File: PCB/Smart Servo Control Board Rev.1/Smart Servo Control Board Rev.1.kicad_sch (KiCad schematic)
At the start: 39 parts

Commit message: salvataggio layout board
tornare a questo salvataggio per riprovare.
piani potenza interni e piani segnali esterni, da scambiare ?
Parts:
- removed J? (x2): CTRL, symbol Connector:Conn_01x04_Female
- removed J?: PRGR, symbol Connector:Conn_01x04_Female
- added J1: PRGR, Connector_PinSocket_2.54mm:PinSocket_1x04_P2.54mm_Vertical, symbol Connector:Conn_01x04_Female
- added J2, J3: CTRL, Connector_PinSocket_2.54mm:PinSocket_1x04_P2.54mm_Vertical, symbol Connector:Conn_01x04_Female
- C1, C10, C11, C12, C14, C2, C3, C4, C5, C6, C7, C8, C9: renamed from C?; footprint Capacitor_SMD:C_0603_1608Metric -> Capacitor_SMD:C_0603_1608Metric_Pad1.08x0.95mm_HandSolder
- C13: renamed from C?; footprint (none) -> Capacitor_SMD:C_0603_1608Metric_Pad1.08x0.95mm_HandSolder
- J4, J5: renamed from J?; footprint (none) -> Connector_PinSocket_2.54mm:PinSocket_1x01_P2.54mm_Vertical
- R1, R2, R3, R5, R6, R7, R8, R9: renamed from R?; footprint (none) -> Resistor_SMD:R_0603_1608Metric_Pad0.98x0.95mm_HandSolder
- R4: renamed from R?; footprint (none) -> Resistor_SMD:R_1206_3216Metric_Pad1.30x1.75mm_HandSolder
- U5, U6, U7: renamed from U?; footprint (none) -> Package_SO:SOIC-8_3.9x4.9mm_P1.27mm
- gave numbers to parts that had none: 6
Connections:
- net +3V3: now also C11.2, C12.2, U4.2 (A0); no longer C11.1, C12.1, U4.1 (A1)
- net +5V: now also J1.4 (Pin_4), J2.4 (Pin_4), J3.4 (Pin_4)
- net A: now also U2.29 (PA8)
- net B: now also U2.31 (PA10)
- net GNDD: now also C11.1, C12.1, U4.1 (A1), J1.1 (Pin_1), J2.1 (Pin_1), J3.1 (Pin_1); no longer C11.2, C12.2, U4.2 (A0)
- net SCL1: now also U2.42 (PB6)
- net SCL2: now also U2.21 (PB10), J2.3 (Pin_3), J3.3 (Pin_3)
- net SDA1: now also U2.43 (PB7)
- net SDA2: now also U2.22 (PB11), J2.2 (Pin_2), J3.2 (Pin_2)
- net SWDCLK: now also J1.2 (Pin_2)
- net SWDIO: now also J1.3 (Pin_3)
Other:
- moved on the sheet: C11, C12

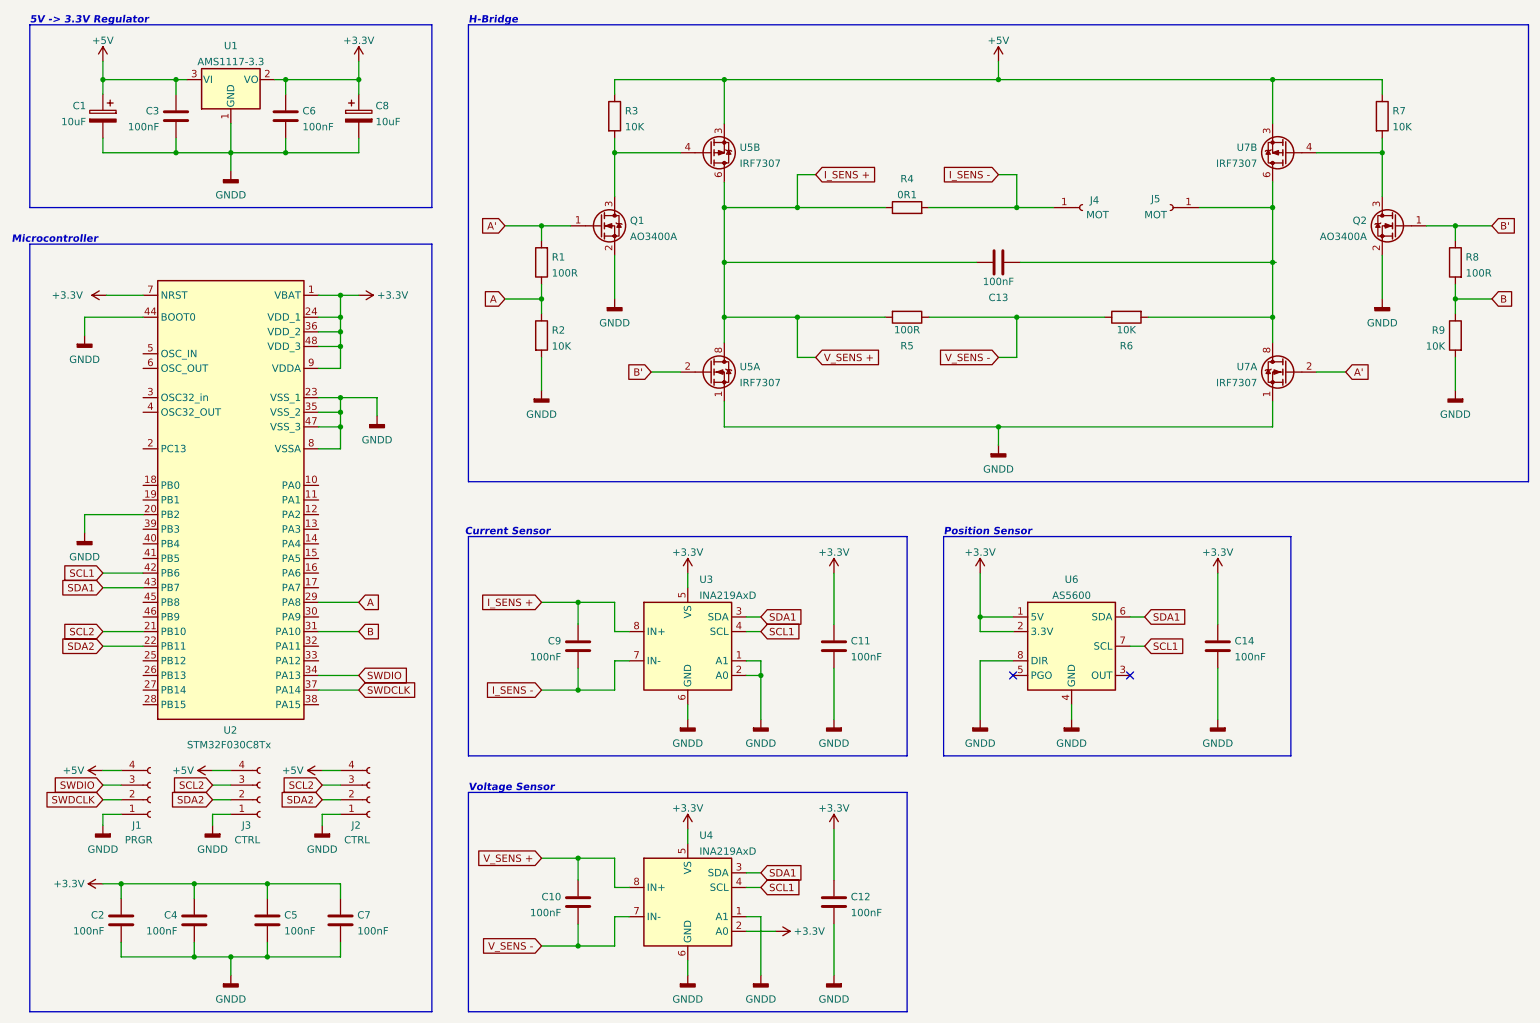
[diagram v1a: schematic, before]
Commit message: Prima versione definitiva PCB
tracciate le piste nel modo migliore possibile per ora, resta da sistemare il silkscreen.
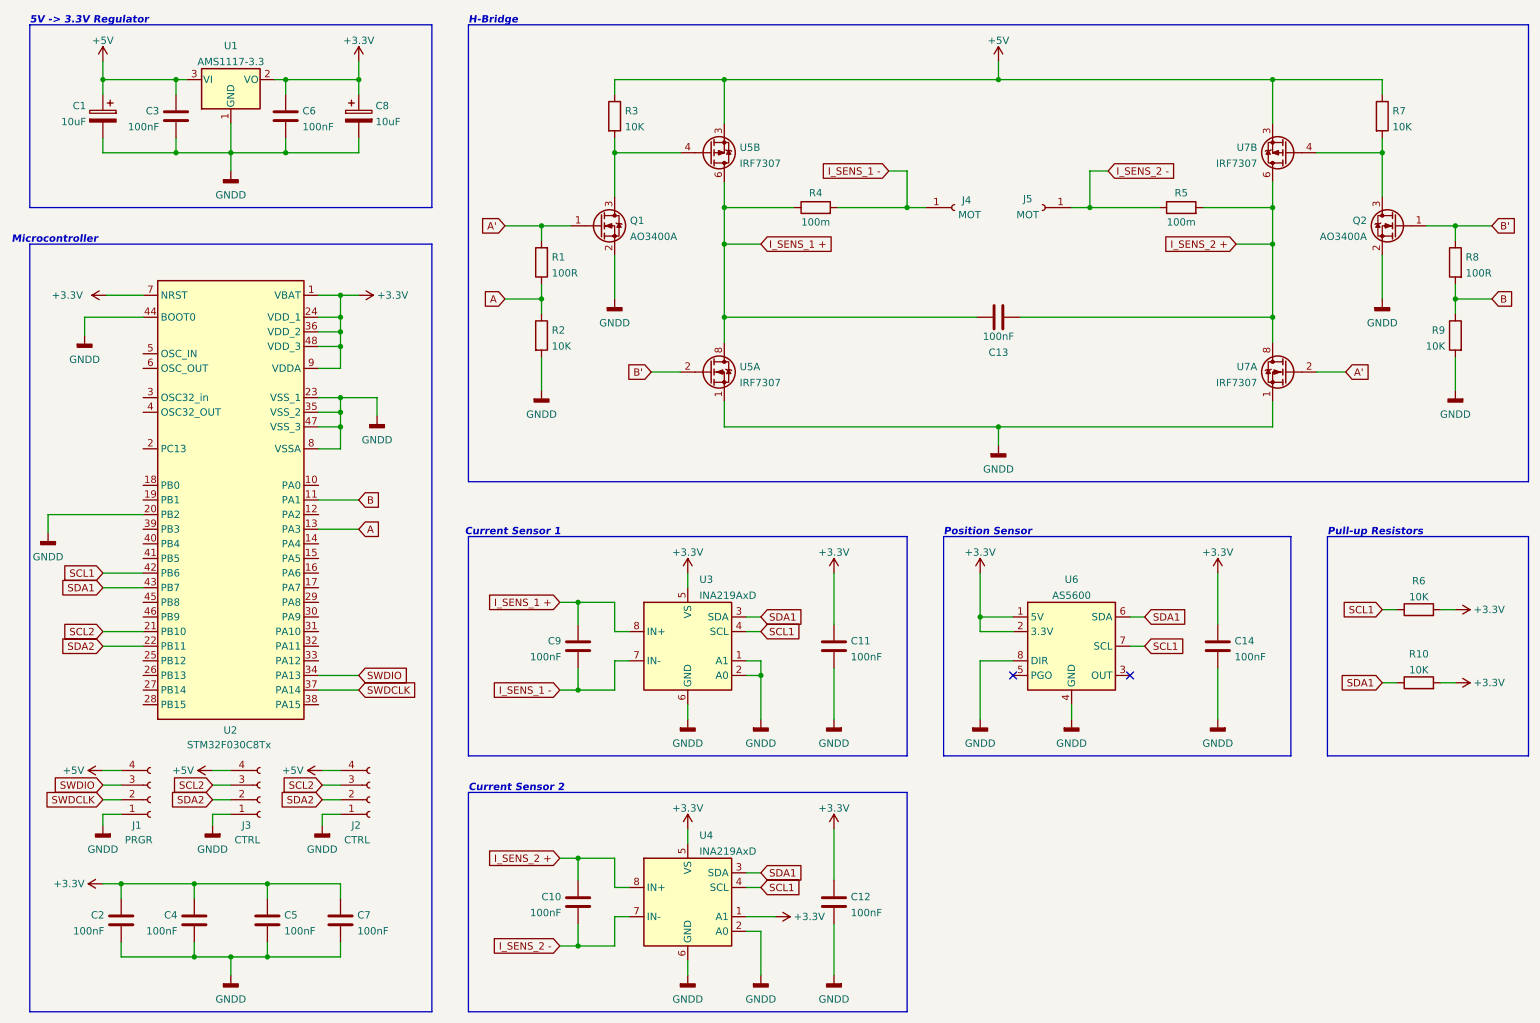
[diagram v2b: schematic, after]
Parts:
- added R10: 10K, Resistor_SMD:R_0603_1608Metric_Pad0.98x0.95mm_HandSolder, symbol Device:R
- R4: value 0R1 -> 100m
- R5: value 100R -> 100m; footprint Resistor_SMD:R_0603_1608Metric_Pad0.98x0.95mm_HandSolder -> Resistor_SMD:R_1206_3216Metric_Pad1.30x1.75mm_HandSolder
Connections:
- net +3V3: now also R6.2, U4.1 (A1), R10.2; no longer U4.2 (A0)
- net A: now also U2.13 (PA3); no longer U2.29 (PA8)
- net B: now also U2.11 (PA1); no longer U2.31 (PA10)
- net GNDD: now also U4.2 (A0); no longer U4.1 (A1)
- net SCL1: now also R6.1
- net SDA1: now also R10.1
- net I_SENS_2 +: now reaches C13.2, U7.5, U7.6, U7.7, U7.8
- net I_SENS_2 +: now also C10.1, R5.2, U4.8 (IN+); no longer J5.1 (Pin_1), R6.2
- net I_SENS + renamed I_SENS_1 +
- net I_SENS_1 +: no longer C10.1, R5.2, U4.8 (IN+)
- net I_SENS - renamed I_SENS_1 -
- net V_SENS - renamed I_SENS_2 -
- net I_SENS_2 -: now also J5.1 (Pin_1); no longer R6.1
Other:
- note added: "Current Sensor 1"
- note added: "Current Sensor 2"
- note added: "Pull-up Resistors"
- note removed: "Current Sensor"
- note removed: "Voltage Sensor"
- moved on the sheet: C13, J4, J5, R4

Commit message: Aggiunti datasheet componenti e aggiunta EEPROM
aggiunto chip EEPROMi2c e datasheet per INA219 e 24LC256.
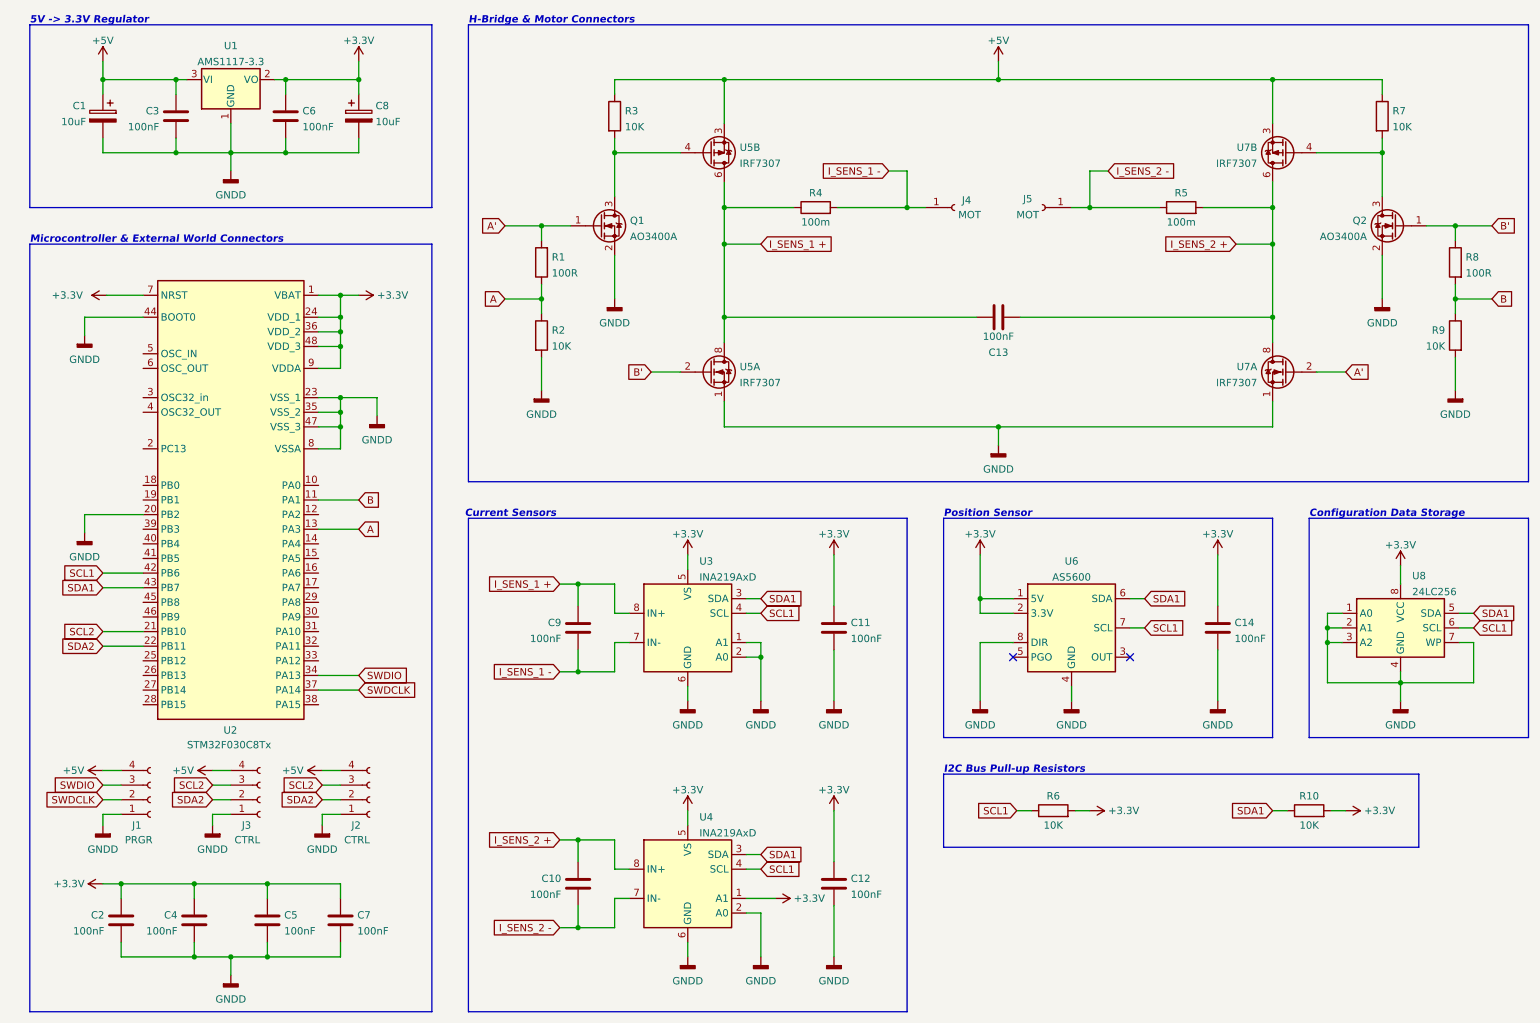
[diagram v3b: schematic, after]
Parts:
- added U8: 24LC256, Package_SO:SOIC-8_3.9x4.9mm_P1.27mm, symbol Memory_EEPROM:24LC256
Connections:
- net +3V3: now also U8.8 (VCC)
- net GNDD: now also U8.1 (A0), U8.2 (A1), U8.3 (A2), U8.4 (GND), U8.7 (WP)
- net SCL1: now also U8.6 (SCL)
- net SDA1: now also U8.5 (SDA)
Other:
- note added: "Configuration Data Storage"
- note added: "Current Sensors"
- note added: "H-Bridge & Motor Connectors"
- note added: "I2C Bus Pull-up Resistors"
- note added: "Microcontroller & External World Connectors"
- note removed: "Current Sensor 1"
- note removed: "Current Sensor 2"
- note removed: "H-Bridge"
- note removed: "Microcontroller"
- note removed: "Pull-up Resistors"
- company: (none) -> Phil's Robotics
- title: (none) -> Smart Servo Control Board
- moved on the sheet: C10, C11, C12, C14, C9, R10, R6, U3, U4, U6
